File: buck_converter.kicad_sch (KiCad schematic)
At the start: 44 parts, among them IC1 LM34936RHFR, Q3 CSD17571Q2, Q4 CSD17571Q2, Q5 CSD15571Q2, Q6 CSD15571Q2, Q7 CSD15571Q2

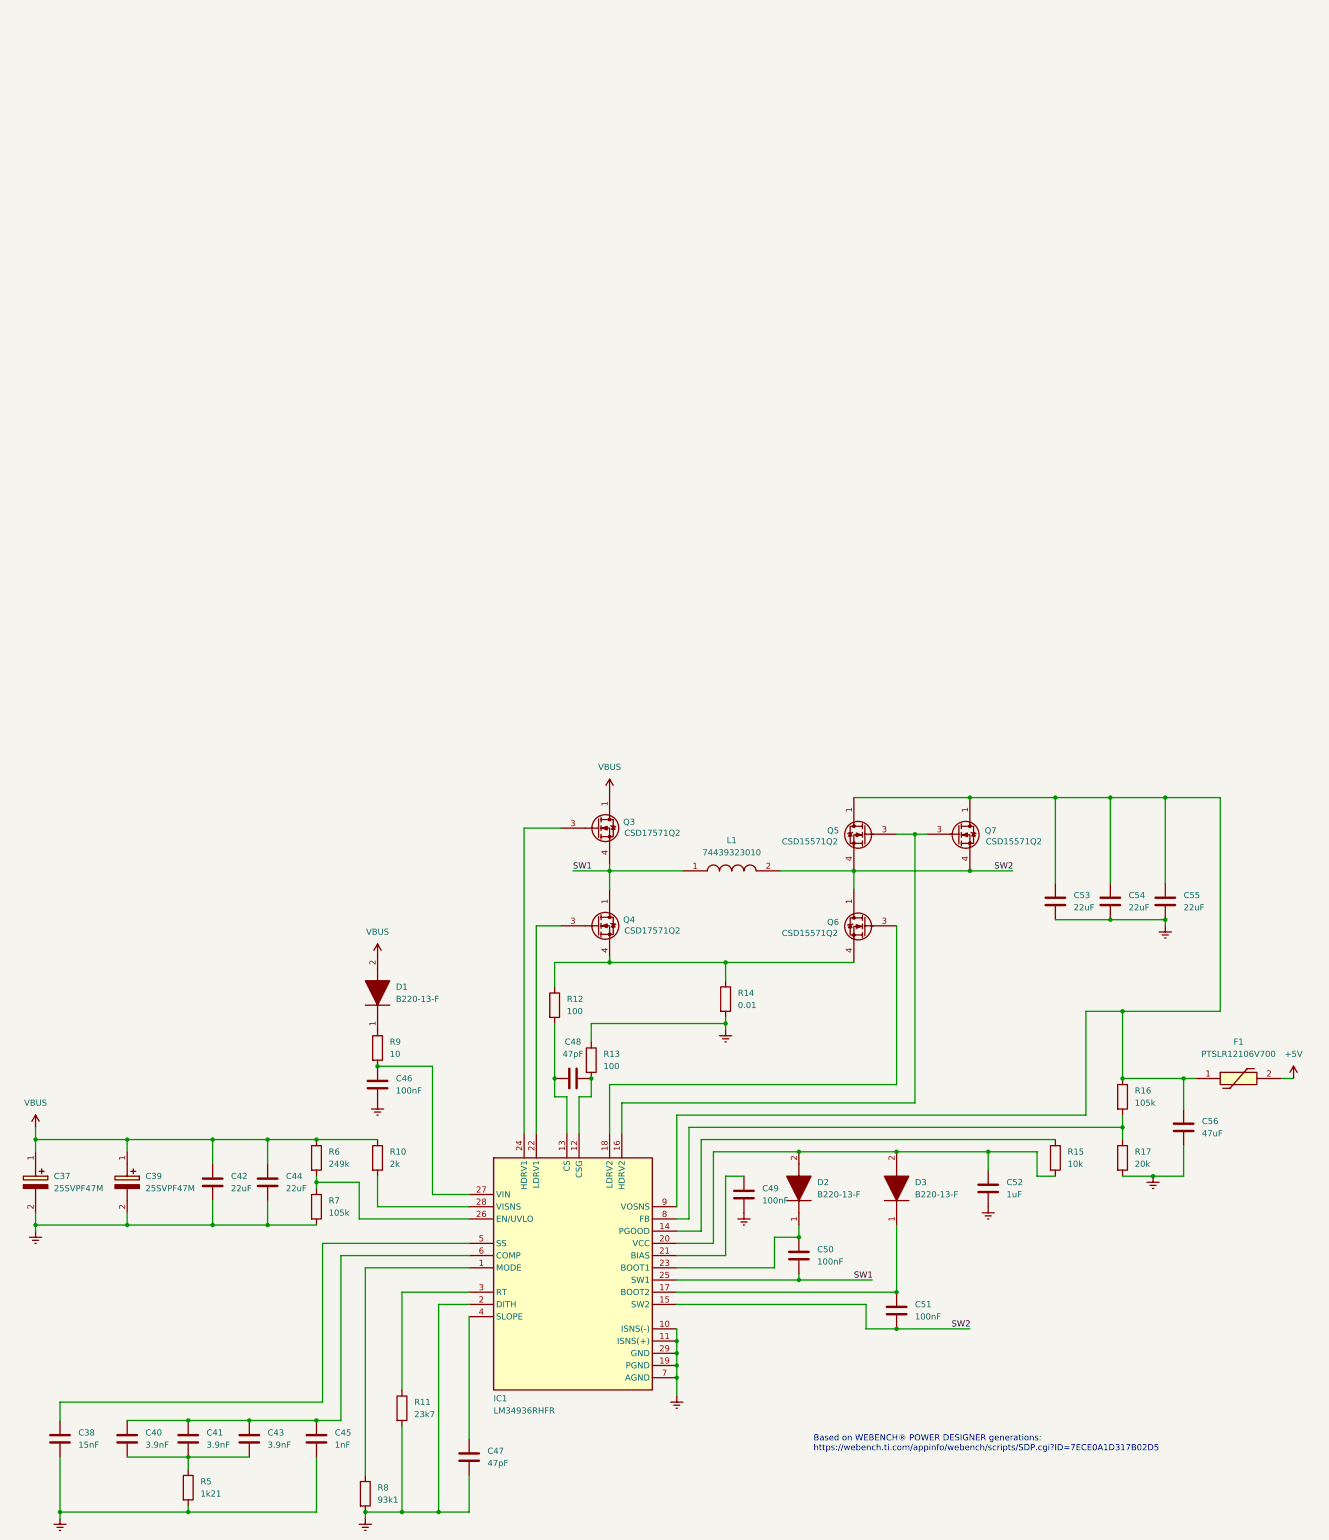
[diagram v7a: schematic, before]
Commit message: 20v to 5v 4A times two
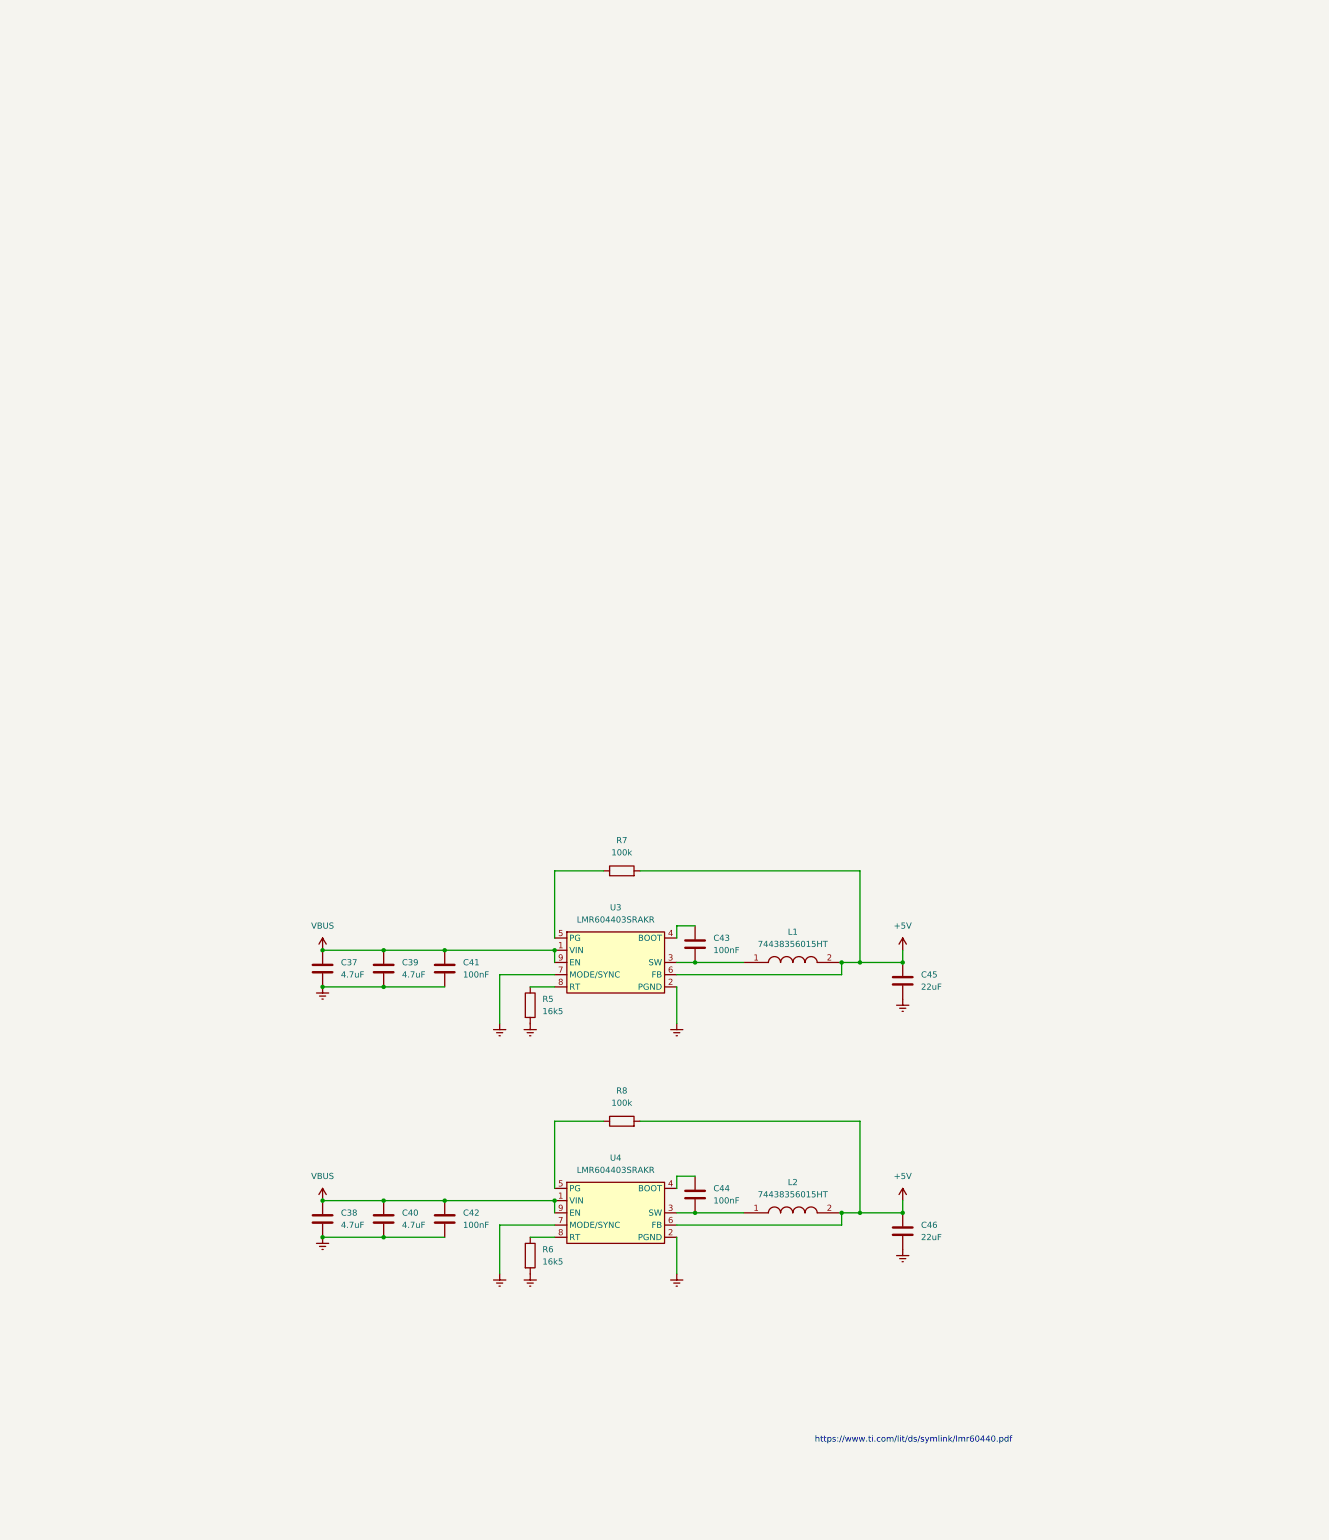
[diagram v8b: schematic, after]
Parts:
- removed C37, C39: 25SVPF47M, 25SVPF47M:16SVF180M, symbol 25SVPF47M:25SVPF47M
- removed C47, C48: 47pF, Capacitor_SMD:C_0603_1608Metric_Pad1.08x0.95mm_HandSolder, symbol Device:C
- removed C49, C50, C51: 100nF, Capacitor_SMD:C_0603_1608Metric_Pad1.08x0.95mm_HandSolder, symbol Device:C
- removed C52: 1uF, Capacitor_SMD:C_0603_1608Metric_Pad1.08x0.95mm_HandSolder, symbol Device:C
- removed C53, C54, C55: 22uF, Capacitor_SMD:C_0603_1608Metric_Pad1.08x0.95mm_HandSolder, symbol Device:C
- removed C56: 47uF, Inductor_SMD:L_1210_3225Metric_Pad1.42x2.65mm_HandSolder, symbol Device:C
- removed D1: B220-13-F, B220-13-F:DIOM5336X250N, symbol B220-13-F:B220-13-F
- removed D2, D3: B220-13-F, DIOM5336X250N, symbol B220-13-F:B220-13-F
- removed F1: PTSLR12106V700, PTSLR12106V700, symbol PTSLR12106V700:PTSLR12106V700
- removed IC1: LM34936RHFR, QFN50P400X500X100-29N-D, symbol LM34936RHFR:LM34936RHFR
- removed L1: 74439323010, 74439323010:74439323010, symbol 74439323010:74439323010
- removed Q3, Q4: CSD17571Q2, CSD25302Q2, symbol CSD17571Q2:CSD17571Q2
- removed Q5: CSD15571Q2, CSD15571Q2:CSD15571Q2, symbol CSD15571Q2:CSD15571Q2
- removed Q6, Q7: CSD15571Q2, CSD15571Q2, symbol CSD15571Q2:CSD15571Q2
- removed R10: 2k, Resistor_SMD:R_0603_1608Metric_Pad0.98x0.95mm_HandSolder, symbol Device:R
- removed R11: 23k7, Resistor_SMD:R_0603_1608Metric_Pad0.98x0.95mm_HandSolder, symbol Device:R
- removed R12, R13: 100, Resistor_SMD:R_0603_1608Metric_Pad0.98x0.95mm_HandSolder, symbol Device:R
- removed R14: 0.01, Resistor_SMD:R_0603_1608Metric_Pad0.98x0.95mm_HandSolder, symbol Device:R
- removed R15: 10k, Resistor_SMD:R_0603_1608Metric_Pad0.98x0.95mm_HandSolder, symbol Device:R
- removed R16: 105k, Resistor_SMD:R_0603_1608Metric_Pad0.98x0.95mm_HandSolder, symbol Device:R
- removed R17: 20k, Resistor_SMD:R_0603_1608Metric_Pad0.98x0.95mm_HandSolder, symbol Device:R
- removed R9: 10, Resistor_SMD:R_0603_1608Metric_Pad0.98x0.95mm_HandSolder, symbol Device:R
- added C37, C39: 4.7uF, Capacitor_SMD:C_0805_2012Metric_Pad1.18x1.45mm_HandSolder, symbol Device:C
- added L1, L2: 74438356015HT, 74438356015HT, symbol 74438356015HT:74438356015HT
- added U3, U4: LMR604403SRAKR, symbol New_Library:LMR604403SRAKR
- C38: value 15nF -> 4.7uF; footprint Capacitor_SMD:C_0603_1608Metric_Pad1.08x0.95mm_HandSolder -> Capacitor_SMD:C_0805_2012Metric_Pad1.18x1.45mm_HandSolder
- C40: value 3.9nF -> 4.7uF
- C41, C43: value 3.9nF -> 100nF; footprint Capacitor_SMD:C_0805_2012Metric_Pad1.18x1.45mm_HandSolder -> Capacitor_SMD:C_0603_1608Metric_Pad1.08x0.95mm_HandSolder
- C42, C44: value 22uF -> 100nF; footprint Inductor_SMD:L_1210_3225Metric_Pad1.42x2.65mm_HandSolder -> Capacitor_SMD:C_0603_1608Metric_Pad1.08x0.95mm_HandSolder
- C45: value 1nF -> 22uF; footprint Capacitor_SMD:C_0603_1608Metric_Pad1.08x0.95mm_HandSolder -> Capacitor_SMD:C_0805_2012Metric_Pad1.18x1.45mm_HandSolder
- C46: value 100nF -> 22uF; footprint Capacitor_SMD:C_0603_1608Metric_Pad1.08x0.95mm_HandSolder -> Capacitor_SMD:C_0805_2012Metric_Pad1.18x1.45mm_HandSolder
- R5: value 1k21 -> 16k5
- R6: value 249k -> 16k5
- R7: value 105k -> 100k
- R8: value 93k1 -> 100k
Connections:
- net +5V: now also C45.1, C46.1, R7.2, R8.2, L1.2, L2.2, U3.6 (FB), U4.6 (FB)
- net GND: now also C40.2, C41.2, R6.2, C37.2, C39.2, U3.2 (PGND), U3.7 (MODE/SYNC), U4.2 (PGND), U4.7 (MODE/SYNC); no longer C44.2, R7.2, R8.2
- net VBUS: now also C38.1, C40.1, C41.1, C37.1, C39.1, U3.1 (VIN), U3.9 (EN), U4.1 (VIN), U4.9 (EN); no longer C44.1, R6.1
- net at R7.1: now also U3.5 (PG); no longer R6.2
- net at R8.1: now also U4.5 (PG)
- new net: C43.1, U3.4 (BOOT)
- new net: C43.2, L1.1, U3.3 (SW)
- new net: C44.1, U4.4 (BOOT)
- new net: C44.2, L2.1, U4.3 (SW)
- new net: R6.1, U4.8 (RT)
- new net: R5.1, U3.8 (RT)
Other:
- note added: "https://www.ti.com/lit/ds/symlink/lmr60440.pdf"
- note removed: "Based on WEBENCH® POWER DESIGNER generations: https://webench.ti.com/appinfo/webench/scripts/SDP.cgi?ID=7ECE0A1D317B02D5"
